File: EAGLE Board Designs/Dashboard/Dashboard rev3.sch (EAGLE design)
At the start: 62 parts, among them J1 AVR-ISP-HEADER, J2 JUMPER0603, X1 CONNECTOR-4NANO-FIT_RIGHT_ANG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, X2 CONNECTOR-6NANO-FIT_RIGHT_ANG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, X3 CONNECTOR-4NANO-FIT_RIGHT_ANG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, X4 CONNECTOR-4NANO-FIT_RIGHT_ANG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

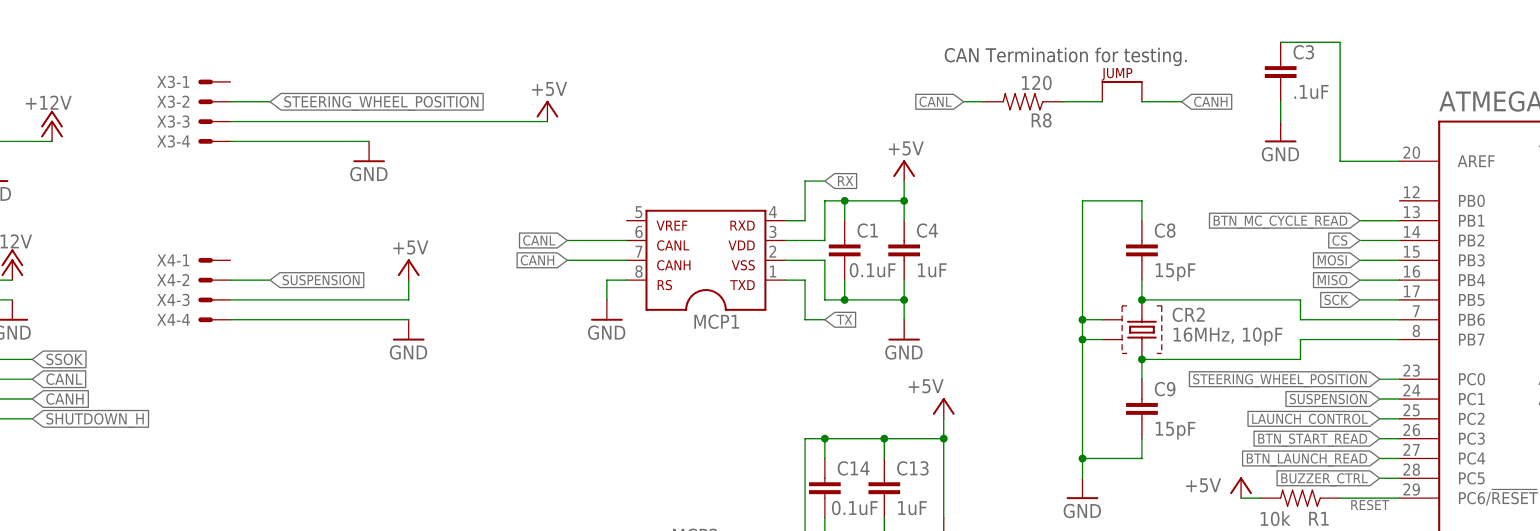
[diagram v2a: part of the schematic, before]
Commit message: Minor deletions because of the sensor board
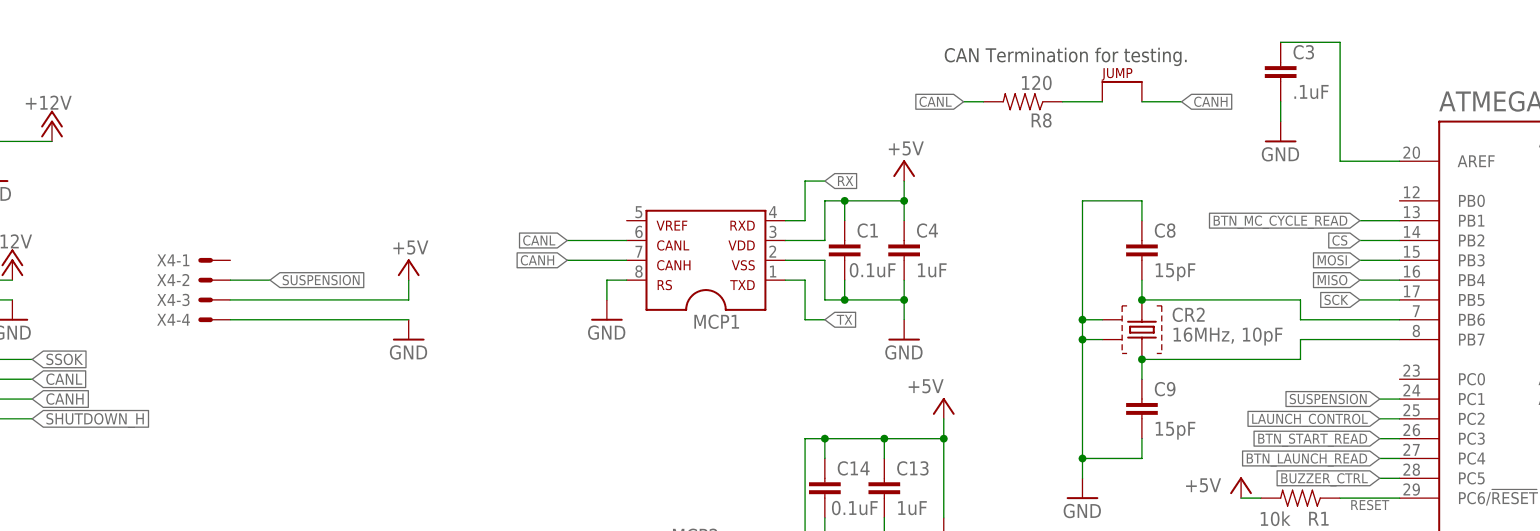
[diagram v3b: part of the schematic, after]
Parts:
- removed X3: CONNECTOR-4NANO-FIT_RIGHT_ANGLE-4-SURFACE, HyTechDevices:CONNECTOR-4NANO-FIT_RIGHT_ANGLE-4-SURFACE
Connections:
- removed net STEERING_WHEEL_POSITION: ATMEGA.PC0, X3-2.S
- net +5V: no longer X3-3.S
- net GND: no longer X3-4.S
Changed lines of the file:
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@@
 <part name="P+12" library="supply1" deviceset="+12V" device=""/>
 <part name="GND18" library="HyTechSymbols" deviceset="GND" device=""/>
-<part name="X3" library="HyTechDevices" deviceset="CONNECTOR-4" device="NANO-FIT_RIGHT_ANGLE-4-SURFACE"/>
-<part name="GND19" library="HyTechSymbols" deviceset="GND" device=""/>
 <part name="X4" library="HyTechDevices" deviceset="CONNECTOR-4" device="NANO-FIT_RIGHT_ANGLE-4-SURFACE"/>
-<part name="P+14" library="supply1" deviceset="+5V" device=""/>
 <part name="GND20" library="HyTechSymbols" deviceset="GND" device=""/>
 <part name="P+13" library="supply1" deviceset="+5V" device=""/>
@@
 <attribute name="VALUE" x="35.56" y="170.18" size="1.778" layer="96"/>
 </instance>
-<instance part="X3" gate="-1" x="63.5" y="203.2" smashed="yes" rot="R180">
-<attribute name="NAME" x="60.96" y="203.962" size="1.524" layer="95" rot="R180"/>
-</instance>
-<instance part="X3" gate="-2" x="63.5" y="200.66" smashed="yes" rot="R180">
-<attribute name="NAME" x="60.96" y="201.422" size="1.524" layer="95" rot="R180"/>
-</instance>
-<instance part="X3" gate="-3" x="63.5" y="198.12" smashed="yes" rot="R180">
-<attribute name="NAME" x="60.96" y="198.882" size="1.524" layer="95" rot="R180"/>
-</instance>
-<instance part="X3" gate="-4" x="63.5" y="195.58" smashed="yes" rot="R180">
-<attribute name="NAME" x="60.96" y="196.342" size="1.524" layer="95" rot="R180"/>
-</instance>
-<instance part="GND19" gate="1" x="83.82" y="193.04" smashed="yes">
-<attribute name="VALUE" x="81.28" y="190.5" size="1.778" layer="96"/>
-</instance>
 <instance part="X4" gate="-1" x="63.5" y="180.34" smashed="yes" rot="R180">
 <attribute name="NAME" x="60.96" y="181.102" size="1.524" layer="95" rot="R180"/>
@@
 <instance part="X4" gate="-4" x="63.5" y="172.72" smashed="yes" rot="R180">
 <attribute name="NAME" x="60.96" y="173.482" size="1.524" layer="95" rot="R180"/>
-</instance>
-<instance part="P+14" gate="1" x="106.68" y="200.66" smashed="yes">
-<attribute name="VALUE" x="109.22" y="203.2" size="1.778" layer="96" rot="R180"/>
 </instance>
 <instance part="GND20" gate="1" x="88.9" y="170.18" smashed="yes">
@@
 </segment>
 <segment>
-<pinref part="X3" gate="-4" pin="S"/>
-<pinref part="GND19" gate="1" pin="GND"/>
-<wire x1="66.04" y1="195.58" x2="83.82" y2="195.58" width="0.1524" layer="91"/>
-</segment>
-<segment>
 <pinref part="X4" gate="-4" pin="S"/>
 <wire x1="66.04" y1="172.72" x2="88.9" y2="172.72" width="0.1524" layer="91"/>
@@
 </segment>
 <segment>
-<pinref part="X3" gate="-3" pin="S"/>
-<wire x1="66.04" y1="198.12" x2="106.68" y2="198.12" width="0.1524" layer="91"/>
-<pinref part="P+14" gate="1" pin="+5V"/>
-</segment>
-<segment>
 <pinref part="X4" gate="-3" pin="S"/>
 <wire x1="66.04" y1="175.26" x2="88.9" y2="175.26" width="0.1524" layer="91"/>
@@
 </segment>
 </net>
-<net name="STEERING_WHEEL_POSITION" class="0">
-<segment>
-<pinref part="X3" gate="-2" pin="S"/>
-<wire x1="66.04" y1="200.66" x2="71.12" y2="200.66" width="0.1524" layer="91"/>
-<label x="71.12" y="200.66" size="1.4224" layer="95" xref="yes"/>
-</segment>
-<segment>
-<pinref part="ATMEGA" gate="G$1" pin="PC0"/>
-<wire x1="215.9" y1="165.1" x2="213.36" y2="165.1" width="0.1524" layer="91"/>
-<label x="213.36" y="165.1" size="1.27" layer="95" rot="R180" xref="yes"/>
-</segment>
-</net>

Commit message: Just working on rev3
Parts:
- removed $$X1: CONNECTOR-8NANO-FIT_VERTICAL-8, HyTechDevices:CONNECTOR-8NANO-FIT_VERTICAL-8
- removed C13: 1uF, HyTechDevices:CAP0603-CAP
- removed C14: 0.1uF, HyTechDevices:CAP0603-CAP
- removed D4: DIODE_ZENER, HyTechDevices:DIODE_ZENER
- removed MCP2: MCP2515TSSOP, HyTechDevices:MCP2515TSSOP
- removed R16: 10k, HyTechDevices:YC248-JR-0710KL
- removed R19: 10k, HyTechDevices:RESISTOR0603
- added C15: 1uF, HyTechDevices:CAP0603-CAP
- added C16: 0.1uF, HyTechDevices:CAP0603-CAP
- added R11, R9: 100, HyTechDevices:CAT16-F4_1%
- added U$2: MCP2518FD, HyTechDevices:MCP2518FD
- added U$3, U$4, U$5, U$6: TVS_DIODE, HyTechDevices:TVS_DIODE
- added X3: CONNECTOR-4NANO, HyTechDevices:CONNECTOR-4NANO
- X1: value CONNECTOR-4NANO-FIT_RIGHT_ANGLE-4-SURFACE -> CONNECTOR-8NANO; device HyTechDevices:CONNECTOR-4NANO-FIT_RIGHT_ANGLE-4-SURFACE -> HyTechDevices:CONNECTOR-8NANO
- X2: value CONNECTOR-6NANO-FIT_RIGHT_ANGLE-6-SURFACE -> CONNECTOR-4NANO; device HyTechDevices:CONNECTOR-6NANO-FIT_RIGHT_ANGLE-6-SURFACE -> HyTechDevices:CONNECTOR-4NANO
- X4: value CONNECTOR-4NANO-FIT_RIGHT_ANGLE-4-SURFACE -> CONNECTOR-6NANO; device HyTechDevices:CONNECTOR-4NANO-FIT_RIGHT_ANGLE-4-SURFACE -> HyTechDevices:CONNECTOR-6NANO
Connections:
- removed net N$1: MCP2.RSTN, R19.1
- removed net N$3: C11.2, CR1.1, MCP2.OSC2
- new net N$30: C11.2, CR1.1, U$2.OSC2
- net +12V: now also U$3.C, X1-1.S, X3-3.S, X4-1.S; no longer $$X1-1.S, X1-3.S, X2-1.S
- net +5V: now also C15.1, C16.1, U$2.VDD, X2-2.S; no longer AMS.A, C13.1, C14.1, IMD.A, MC.A, MCP2.VDD, MODE.A, R19.2, START.A, X4-3.S
- net +5V1: now also AMS.A, IMD.A, MC.A, MODE.A, START.A
- net BTN_LAUNCH_READ: now also X1-7.S; no longer $$X1-7.S
- net BTN_MARK_READ: now also X1-2.S; no longer $$X1-2.S
- net BTN_MC_CYCLE_READ: now also X1-3.S; no longer $$X1-3.S
- net BTN_MODE_READ: now also X1-5.S; no longer $$X1-5.S
- net BTN_START_READ: now also X1-6.S; no longer $$X1-6.S
- net BUZZER_CTRL: now also R11_3.2, U$6.C; no longer D4.C, R16F.1
- net BUZZER_OUT: now also X1-4.S; no longer $$X1-4.S
- net CANH: now also X3-2.S, X4-5.S; no longer X1-2.S, X2-5.S
- net CANL: now also X3-1.S, X4-4.S; no longer X1-1.S, X2-4.S
- net CS: now also U$2.!CS; no longer MCP2.CS
- net GND: now also C15.2, C16.2, R11_1.1, R11_3.1, R9_1.1, R9_2.1, R9_3.1, R9_4.1, U$2.GND, U$3.A, U$6.A, X1-8.S, X2-3.S, X3-4.S, X4-2.S; no longer $$X1-8.S, C13.2, C14.2, D4.A, MCP2.VSS, R16A.2, R16B.2, R16C.2, R16D.2, R16E.2, R16F.2, X1-4.S, X2-2.S, X4-4.S
- net GND1: now also R11_2.1; no longer R16G.1
- net LED_AMS_CTRL: now also R11_1.2; no longer R16E.1
- net LED_IMD_CTRL: now also R9_4.2; no longer R16D.1
- net LED_LAUNCH_CTRL: now also R11_2.2; no longer R16G.2
- net LED_MC_ERR_CTRL: now also R9_2.2; no longer R16B.1
- net LED_MODE_CTRL: now also R9_3.2; no longer R16C.1
- net LED_START_CTRL: now also R9_1.2; no longer R16A.1
- net MISO: now also U$2.SDO; no longer MCP2.SO
- net MOSI: now also U$2.SDI; no longer MCP2.SI
- net N$2: now also U$2.OSC1; no longer MCP2.OSC1
- net RX: now also U$2.RX; no longer MCP2.RXCAN
- net SCK: now also U$2.CLK; no longer MCP2.SCK
- net SHUTDOWN_H: now also X4-6.S; no longer X2-6.S
- net SSOK: now also X4-3.S; no longer X2-3.S
- net SUSPENSION: now also X2-1.S; no longer X4-2.S
- net TX: now also U$2.TX; no longer MCP2.TXCAN
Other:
- moved on the sheet: C1, C11, C4, C6, CR1, MCP1, X1-1, X1-2, X1-3, X1-4, X2-1, X2-2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

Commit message: Dashboard rev3
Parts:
- removed U$4, U$5: TVS_DIODE, HyTechDevices:TVS_DIODE
- removed X2: CONNECTOR-4NANO, HyTechDevices:CONNECTOR-4NANO
- R11, R9: value 100 -> 10k
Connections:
- removed net LAUNCH_CONTROL: ATMEGA.PC2
- removed net SUSPENSION: ATMEGA.PC1, X2-1.S
- net +5V: no longer X2-2.S
- net GND: no longer X2-3.S
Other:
- note added: "Gate resistor here ->"
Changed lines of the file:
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@@
 <part name="P+12" library="supply1" deviceset="+12V" device=""/>
 <part name="GND18" library="HyTechSymbols" deviceset="GND" device=""/>
-<part name="GND20" library="HyTechSymbols" deviceset="GND" device=""/>
-<part name="P+13" library="supply1" deviceset="+5V" device=""/>
 <part name="X1" library="HyTechDevices" deviceset="CONNECTOR-8" device="NANO"/>
 <part name="X3" library="HyTechDevices" deviceset="CONNECTOR-4" device="NANO"/>
-<part name="X2" library="HyTechDevices" deviceset="CONNECTOR-4" device="NANO"/>
 <part name="X4" library="HyTechDevices" deviceset="CONNECTOR-6" device="NANO"/>
 <part name="U$2" library="HyTechDevices" deviceset="MCP2518FD" device=""/>
@@
 <part name="GND21" library="HyTechSymbols" deviceset="GND" device=""/>
 <part name="U$3" library="HyTechDevices" deviceset="TVS_DIODE" device=""/>
-<part name="U$4" library="HyTechDevices" deviceset="TVS_DIODE" device=""/>
-<part name="U$5" library="HyTechDevices" deviceset="TVS_DIODE" device=""/>
 <part name="U$6" library="HyTechDevices" deviceset="TVS_DIODE" device=""/>
-<part name="R9" library="HyTechDevices" deviceset="CAT16-*4" device="_1%" technology="F" value="100"/>
-<part name="R11" library="HyTechDevices" deviceset="CAT16-*4" device="_1%" technology="F" value="100"/>
+<part name="R9" library="HyTechDevices" deviceset="CAT16-*4" device="_1%" technology="F" value="10k"/>
+<part name="R11" library="HyTechDevices" deviceset="CAT16-*4" device="_1%" technology="F" value="10k"/>
 </parts>
 <sheets>
@@
 <text x="170.18" y="121.92" size="1.778" layer="97">Voltage regulation for the buzzer.</text>
 <text x="157.48" y="205.74" size="1.778" layer="97">CAN Termination for testing.</text>
+<text x="35.56" y="139.7" size="1.27" layer="91">Gate resistor here -&gt;</text>
 </plain>
 <instances>
@@
 <attribute name="VALUE" x="40.64" y="177.8" size="1.778" layer="96"/>
 </instance>
-<instance part="GND20" gate="1" x="50.8" y="152.4" smashed="yes">
-<attribute name="VALUE" x="48.26" y="149.86" size="1.778" layer="96"/>
-</instance>
-<instance part="P+13" gate="1" x="50.8" y="162.56" smashed="yes">
-<attribute name="VALUE" x="53.34" y="165.1" size="1.778" layer="96" rot="R180"/>
-</instance>
 <instance part="X1" gate="-1" x="83.82" y="195.58" smashed="yes">
 <attribute name="NAME" x="86.36" y="194.818" size="1.524" layer="95"/>
@@
 <attribute name="NAME" x="22.86" y="198.882" size="1.524" layer="95" rot="R180"/>
 </instance>
-<instance part="X2" gate="-1" x="25.4" y="160.02" smashed="yes" rot="R180">
-<attribute name="NAME" x="22.86" y="160.782" size="1.524" layer="95" rot="R180"/>
-<attribute name="VALUE" x="5.842" y="161.163" size="1.778" layer="96"/>
-</instance>
-<instance part="X2" gate="-2" x="25.4" y="157.48" smashed="yes" rot="R180">
-<attribute name="NAME" x="22.86" y="158.242" size="1.524" layer="95" rot="R180"/>
-</instance>
-<instance part="X2" gate="-3" x="25.4" y="154.94" smashed="yes" rot="R180">
-<attribute name="NAME" x="22.86" y="155.702" size="1.524" layer="95" rot="R180"/>
-</instance>
-<instance part="X2" gate="-4" x="25.4" y="152.4" smashed="yes" rot="R180">
-<attribute name="NAME" x="22.86" y="153.162" size="1.524" layer="95" rot="R180"/>
-</instance>
 <instance part="X4" gate="-1" x="25.4" y="185.42" smashed="yes" rot="R180">
 <attribute name="NAME" x="22.86" y="186.182" size="1.524" layer="95" rot="R180"/>
@@
 <attribute name="NAME" x="49.0474" y="181.61" size="1.778" layer="95" rot="R90"/>
 <attribute name="VALUE" x="54.3814" y="181.61" size="1.778" layer="96" rot="R90"/>
-</instance>
-<instance part="U$4" gate="G$1" x="33.02" y="358.14" smashed="yes" rot="R90">
-<attribute name="NAME" x="31.2674" y="354.33" size="1.778" layer="95" rot="R90"/>
-<attribute name="VALUE" x="36.6014" y="354.33" size="1.778" layer="96" rot="R90"/>
-</instance>
-<instance part="U$5" gate="G$1" x="33.02" y="360.68" smashed="yes" rot="R90">
-<attribute name="NAME" x="31.2674" y="356.87" size="1.778" layer="95" rot="R90"/>
-<attribute name="VALUE" x="36.6014" y="356.87" size="1.778" layer="96" rot="R90"/>
 </instance>
 <instance part="U$6" gate="G$1" x="66.04" y="12.7" smashed="yes" rot="R90">
@@
 </segment>
 <segment>
-<wire x1="27.94" y1="154.94" x2="50.8" y2="154.94" width="0.1524" layer="91"/>
-<pinref part="GND20" gate="1" pin="GND"/>
-<pinref part="X2" gate="-3" pin="S"/>
-</segment>
-<segment>
 <wire x1="119.38" y1="119.38" x2="116.84" y2="119.38" width="0.1524" layer="91"/>
 <wire x1="116.84" y1="119.38" x2="116.84" y2="116.84" width="0.1524" layer="91"/>
@@
 <pinref part="J1" gate="G$1" pin="2"/>
 <wire x1="241.3" y1="66.04" x2="238.76" y2="66.04" width="0.1524" layer="91"/>
-</segment>
-<segment>
-<wire x1="27.94" y1="157.48" x2="50.8" y2="157.48" width="0.1524" layer="91"/>
-<wire x1="50.8" y1="157.48" x2="50.8" y2="160.02" width="0.1524" layer="91"/>
-<pinref part="P+13" gate="1" pin="+5V"/>
-<pinref part="X2" gate="-2" pin="S"/>
 </segment>
 <segment>
@@
 </segment>
 </net>
-<net name="SUSPENSION" class="0">
-<segment>
-<pinref part="ATMEGA" gate="G$1" pin="PC1"/>
-<wire x1="215.9" y1="162.56" x2="213.36" y2="162.56" width="0.1524" layer="91"/>
-<label x="213.36" y="162.56" size="1.27" layer="95" rot="R180" xref="yes"/>
-</segment>
-<segment>
-<wire x1="27.94" y1="160.02" x2="33.02" y2="160.02" width="0.1524" layer="91"/>
-<label x="33.02" y="160.02" size="1.27" layer="95" xref="yes"/>
-<pinref part="X2" gate="-1" pin="S"/>
-</segment>
-</net>
-<net name="LAUNCH_CONTROL" class="0">
-<segment>
-<pinref part="ATMEGA" gate="G$1" pin="PC2"/>
-<wire x1="215.9" y1="160.02" x2="213.36" y2="160.02" width="0.1524" layer="91"/>
-<label x="213.36" y="160.02" size="1.27" layer="95" rot="R180" xref="yes"/>
-</segment>
-</net>
